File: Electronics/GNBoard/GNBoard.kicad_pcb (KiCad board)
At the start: 2 copper layers, 14 parts, among them P1 Battery, SW1 PowerSwitch, U1 LM2576

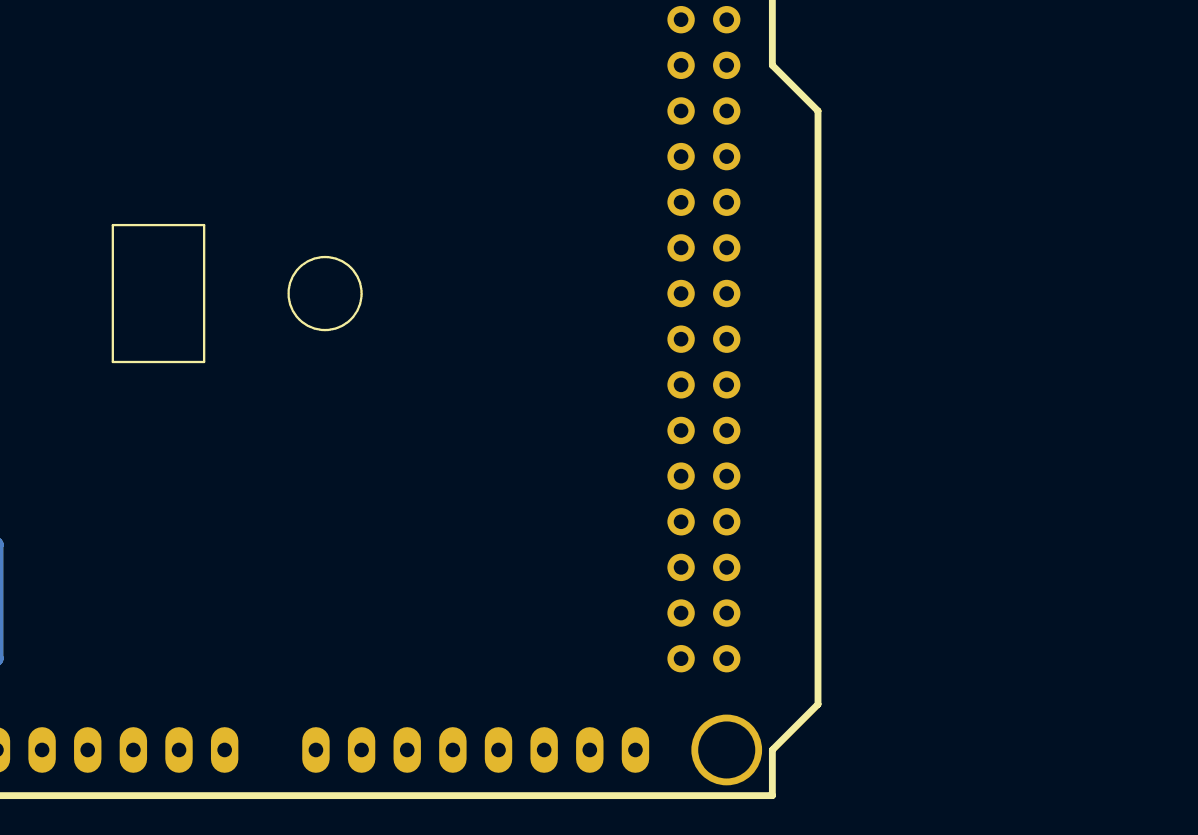
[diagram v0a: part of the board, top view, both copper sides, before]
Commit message: LDR and IR connectors added to schematic
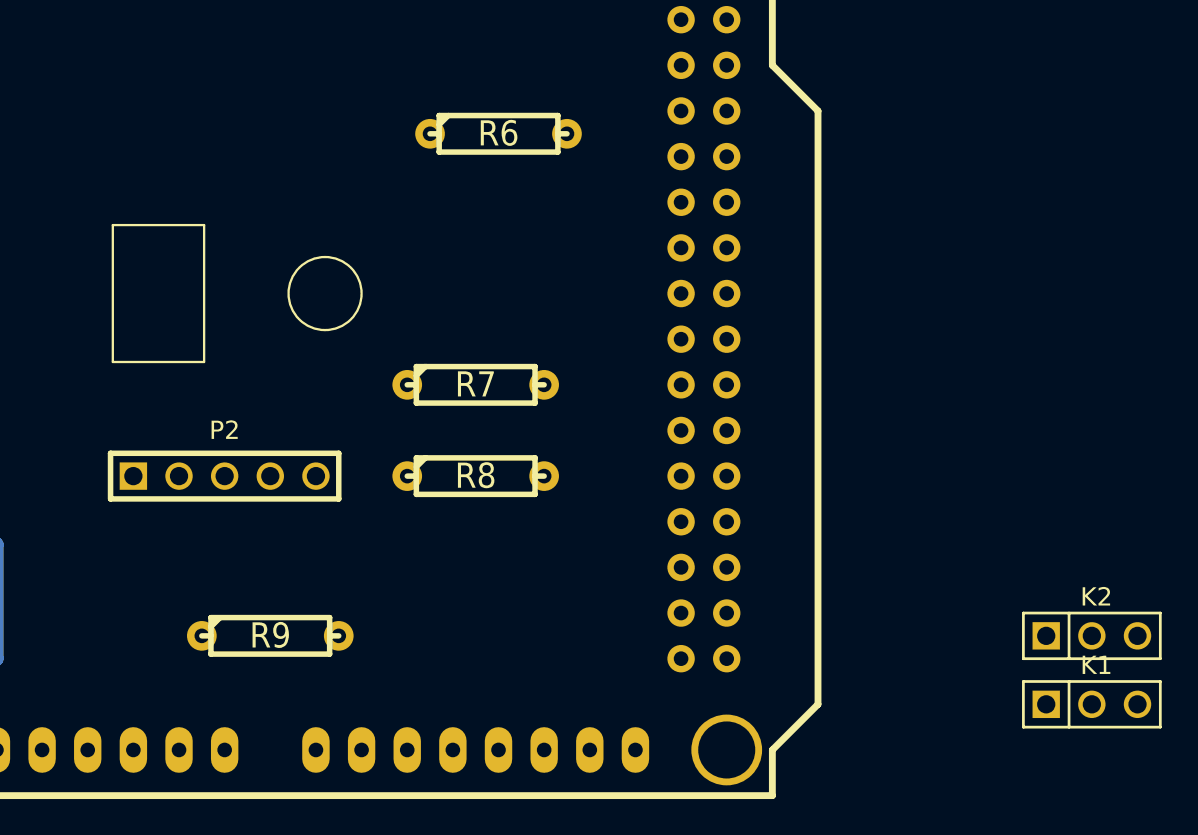
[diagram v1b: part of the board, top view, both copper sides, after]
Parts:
- added K1: IR1, PIN_ARRAY_3X1, F.Cu at (223.5, 118.1)
- added K2: IR2, PIN_ARRAY_3X1, F.Cu at (223.5, 114.3)
- added P2: CONN_5, PIN_ARRAY_5x1, F.Cu at (175.3, 105.4)
- added R6: 33k, R3-LARGE_PADS, F.Cu at (190.5, 86.4)
- added R7: 33k, R3-LARGE_PADS, F.Cu at (189.2, 100.3)
- added R8: 33k, R3-LARGE_PADS, F.Cu at (189.2, 105.4)
- added R9: 33k, R3-LARGE_PADS, F.Cu at (177.8, 114.3)
- R1, R5: value R -> 6k8
- R2, R3, R4: value R -> 330

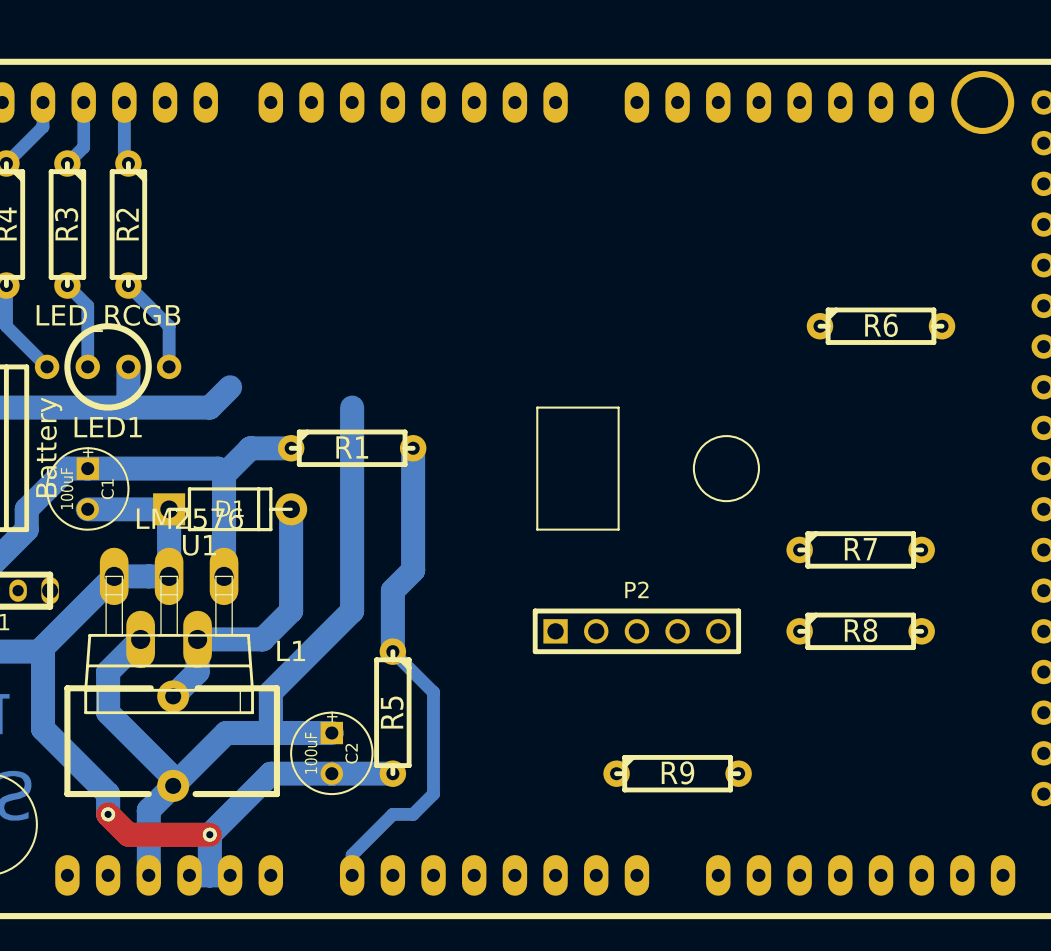
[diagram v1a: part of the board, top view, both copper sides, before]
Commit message: Layout for the LDR
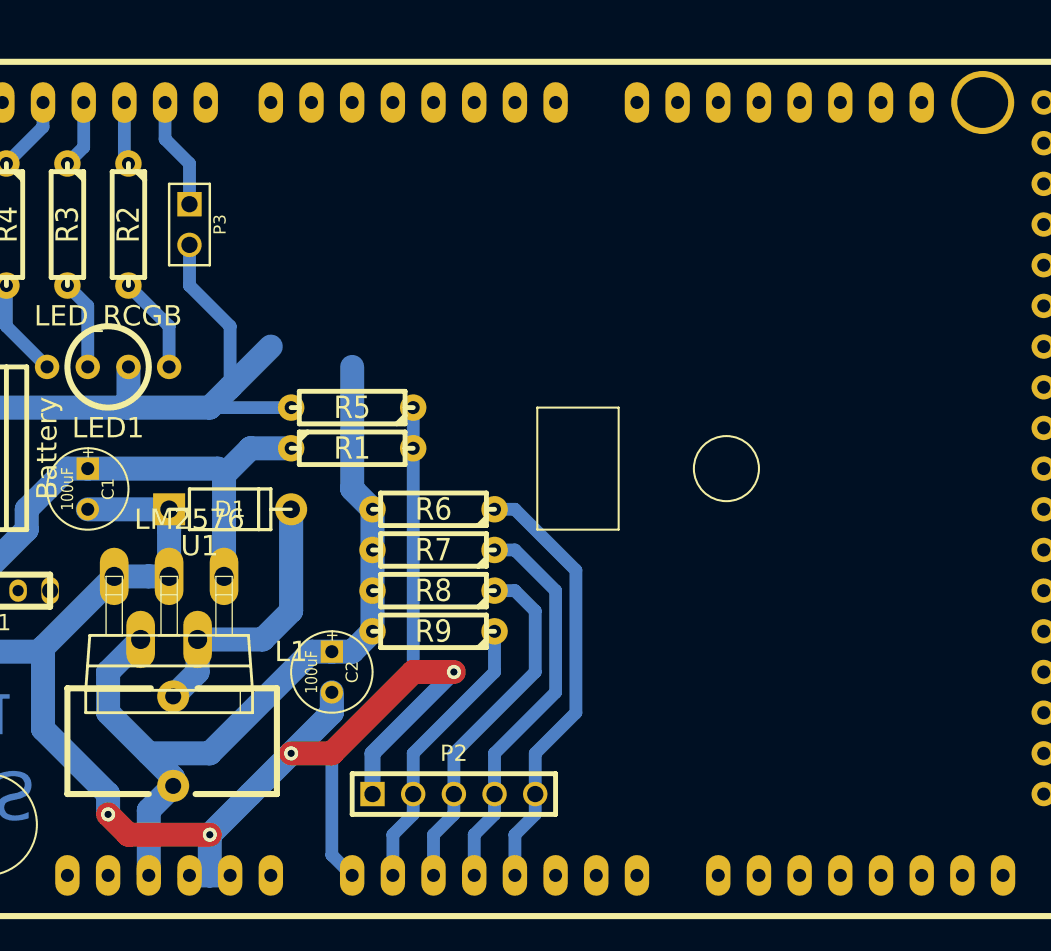
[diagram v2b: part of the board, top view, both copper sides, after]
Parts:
- added P3: Spk, PIN_ARRAY_2X1, F.Cu at (147.3, 80.0)
- moved R6 30.2 mm to (162.6, 97.8), turned to 180 degrees
- moved R8 26.8 mm to (162.6, 102.9), turned to 180 degrees
- moved R7 26.7 mm to (162.6, 100.3), turned to 180 degrees
- moved R5 19.2 mm to (157.5, 91.4), turned to 180 degrees
- moved R9 17.6 mm to (162.6, 105.4), turned to 180 degrees
- moved P2 15.3 mm to (163.8, 115.6)
- moved C2 5.08 mm to (156.2, 108.0)
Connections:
- SHIELD1 pad 9: N-0000046 (its old number) -> Buzzer
- SHIELD1 pad AD1: N-0000065 (its old number) -> LDR1
- SHIELD1 pad AD2: N-0000074 (its old number) -> LDR2
- SHIELD1 pad AD3: N-0000073 (its old number) -> LDR3
- SHIELD1 pad AD4: N-0000071 (its old number) -> LDR4
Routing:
- net GND: track 122.1 -> 161.8 mm, vias 2 -> 4
- net LDR4: track 0.00 -> 27.3 mm
- net LDR3: track 0.00 -> 24.7 mm
- net LDR2: track 0.00 -> 22.2 mm
- net LDR1: track 0.00 -> 17.9 mm
- net Buzzer: track 0.00 -> 6.98 mm
- net BattVolt: track 31.1 -> 31.8 mm
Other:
- net class Default: clearance 0.5 -> 0.4
- rule trace_clearance: 0.5 -> 0.4

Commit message: v0.1 finished
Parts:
- added K10: IR4, PIN_ARRAY_3X1, F.Cu at (179.7, 114.3)
- added K11: CNY_1, PIN_ARRAY_3X1, F.Cu at (173.4, 78.7)
- added K12: CNY_2, PIN_ARRAY_3X1, F.Cu at (175.9, 78.7)
- added K13: CNY_3, PIN_ARRAY_3X1, F.Cu at (178.4, 78.7)
- added K14: CNY_4, PIN_ARRAY_3X1, F.Cu at (181.0, 78.7)
- added K15: CNY_5, PIN_ARRAY_3X1, F.Cu at (183.5, 78.7)
- added K16: CNY_6, PIN_ARRAY_3X1, F.Cu at (186.1, 78.7)
- added K3: SERVO_1, PIN_ARRAY_3X1, F.Cu at (153.7, 78.7)
- added K4: SERVO_2, PIN_ARRAY_3X1, F.Cu at (156.2, 78.7)
- added K5: SERVO_3, PIN_ARRAY_3X1, F.Cu at (158.8, 78.7)
- added K6: SERVO_4, PIN_ARRAY_3X1, F.Cu at (161.3, 78.7)
- added K7: SERVO_5, PIN_ARRAY_3X1, F.Cu at (163.8, 78.7)
- added K8: SERVO_6, PIN_ARRAY_3X1, F.Cu at (166.4, 78.7)
- added K9: IR3, PIN_ARRAY_3X1, F.Cu at (177.2, 114.3)
- added P4: I2C_1, PIN_ARRAY_4x1, F.Cu at (193.7, 76.8)
- added P5: I2C_2, PIN_ARRAY_4x1, F.Cu at (193.7, 85.7)
- added P6: DHT_Conn, PIN_ARRAY_4x1, F.Cu at (191.1, 114.9)
- added R10: R, R3-LARGE_PADS, F.Cu at (193.7, 82.5)
- added R11: R, R3-LARGE_PADS, F.Cu at (193.7, 80.0)
- added R12: 10k, R3-LARGE_PADS, F.Cu at (184.2, 113.7)
- added SW2: SW_PUSH, SW_PUSH_SMALL, F.Cu at (134.6, 81.3)
- added SW3: SW_PUSH, SW_PUSH_SMALL, F.Cu at (133.3, 113.7)
- moved K1 51.6 mm to (172.1, 114.3), turned to 90 degrees
- moved K2 48.9 mm to (174.6, 114.3), turned to 90 degrees
- moved P2 20.7 mm to (167.6, 95.2), turned to 90 degrees
- moved R5 8.03 mm to (149.9, 88.9), turned to 225 degrees
- moved R6 7.73 mm to (161.3, 90.2)
- moved R7 7.73 mm to (161.3, 92.7)
- moved R8 7.73 mm to (161.3, 95.2)
- moved R9 7.73 mm to (161.3, 97.8)
- moved R1 6.35 mm to (152.4, 90.2), turned to 45 degrees
- moved R4 5.08 mm to (141.0, 80.0)
- moved R3 3.81 mm to (143.5, 80.0)
- moved P3 3.59 mm to (149.9, 77.5)
- moved R2 2.54 mm to (146.1, 80.0)
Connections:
- SHIELD1 pad 10: LedR -> LedG
- SHIELD1 pad 11: LedG -> LedB
- SHIELD1 pad 12: LedB -> Button1
- SHIELD1 pad 14: N-0000023 -> CNY1
- SHIELD1 pad 15: N-0000059 -> CNY2
- SHIELD1 pad 16: N-0000055 -> CNY3
- SHIELD1 pad 17: N-0000051 (its old number) -> CNY4
- SHIELD1 pad 18: N-0000047 (its old number) -> CNY5
- SHIELD1 pad 19: N-0000043 -> CNY6
- SHIELD1 pad 2: N-0000060 (its old number) -> Servo6
- SHIELD1 pad 20: N-0000061 -> I2C_SDA
- SHIELD1 pad 21: N-0000036 (its old number) -> I2C_SCL
- SHIELD1 pad 3: N-0000067 -> Servo5
- SHIELD1 pad 4: N-0000066 (its old number) -> Servo4
- SHIELD1 pad 5: N-0000065 -> Servo3
- SHIELD1 pad 6: N-0000064 (its old number) -> Servo2
- SHIELD1 pad 7: N-0000063 -> Servo1
- SHIELD1 pad 8: N-0000062 -> Buzzer
- SHIELD1 pad 9: Buzzer -> LedR
- SHIELD1 pad AD5: N-0000081 -> V_IR1
- SHIELD1 pad AD6: N-0000080 -> V_IR2
- SHIELD1 pad AD7: N-0000079 -> V_IR3
- SHIELD1 pad AD8: N-0000071 (its old number) -> V_IR4
- SHIELD1 pad AD9: N-0000078 (its old number) -> DHTpin
- SHIELD1 pad RST: N-0000077 (its old number) -> ResetB
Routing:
- net GND: track 161.8 -> 345.6 mm
- net +5V: track 52.1 -> 196.1 mm
- net I2C_SCL: track 0.00 -> 16.1 mm
- net I2C_SDA: track 0.00 -> 15.2 mm
- net DHTpin: track 0.00 -> 14.1 mm
- net LDR1: track 17.9 -> 31.4 mm
- net BattVolt: track 31.8 -> 44.8 mm
- net LDR4: track 27.3 -> 39.0 mm
- net LDR3: track 24.7 -> 36.5 mm
- net LDR2: track 22.2 -> 33.9 mm
- net Button1: track 0.00 -> 5.50 mm
- net V_IR1: track 0.00 -> 5.34 mm
- net ResetB: track 0.00 -> 5.13 mm
- net V_IR3: track 0.00 -> 4.60 mm
- net V_IR2: track 0.00 -> 4.60 mm
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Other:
- board outline added: 78.1 x 54.6 mm
- net class Default: via_dia 0.889 -> 1.5; via_drill 0.635 -> 0.6
- board text added: "CGS 2013"
- board text removed: "CGS"

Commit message: Added decoupling caps
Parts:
- added C3: 100uF, C1V7, F.Cu at (196.2, 91.4)
- added C4: 100uF, C1V7, F.Cu at (178.4, 87.0)
- added C5: 100uF, C1V7, F.Cu at (176.5, 106.7)
- added C6: 100uF, C1V7, F.Cu at (181.0, 137.2)
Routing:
- net +5V: track 196.1 -> 207.5 mm
- net GND: track 345.6 -> 351.6 mm

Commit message: Finished first version, added schematics
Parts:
- removed C6: 100uF, C1V7
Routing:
- net +5V: track 207.5 -> 208.1 mm
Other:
- outline, holes or cut-outs redrawn

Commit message: First tests, added source code
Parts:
- C2: value 100uF -> 1000uF; footprint C1V5 -> C1V8
- moved C2 1.27 mm to (157.5, 108.0)
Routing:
- net +5V: track 208.1 -> 208.7 mm
- net GND: track 351.6 -> 352.1 mm
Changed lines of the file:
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@@
     (links 123)
     (no_connects 5)
-    (area 104.010934 64.7256 208.870501 124.015501)
+    (area 125.539499 69.024499 204.025501 124.015501)
     (thickness 1.6)
     (drawings 10)
@@
   )
   (setup
-    (last_trace_width 0.8)
+    (last_trace_width 1.5)
     (user_trace_width 1)
     (user_trace_width 1.5)
@@
   )
   (module C1V5 (layer Comp.)
-    (at 156.21 107.95 270)
-    (descr "Condensateur e = 1 pas")
-    (tags C)
-    (fp_text reference C2 (at 0 -1.26746 270) (layer F.SilkS)
-      (effects (font (size 0.762 0.762) (thickness 0.127)))
-    )
-    (fp_text value 100uF (at 0 1.27 270) (layer F.SilkS)
-      (effects (font (size 0.762 0.635) (thickness 0.127)))
-    )
-    (fp_text user + (at -2.286 0 270) (layer F.SilkS)
-      (effects (font (size 0.762 0.762) (thickness 0.2032)))
-    )
-    (fp_circle (center 0 0) (end 0.127 -2.54) (layer F.SilkS) (width 0.127))
-    (pad 1 thru_hole rect (at -1.27 0 270) (size 1.397 1.397) (drill 0.8128)
-      (layers *.Cu *.Mask F.SilkS)
-      (net 1 +5V)
-    )
-    (pad 2 thru_hole circle (at 1.27 0 270) (size 1.397 1.397) (drill 0.8128)
-      (layers *.Cu *.Mask F.SilkS)
-      (net 13 GND)
-    )
-    (model discret/c_vert_c1v5.wrl
-      (at (xyz 0 0 0))
-      (scale (xyz 1 1 1))
-      (rotate (xyz 0 0 0))
-    )
-  )
-  (module C1V5 (layer Comp.)
     (at 140.97 96.52 270)
     (descr "Condensateur e = 1 pas")
@@
     )
   )
+  (module C1V8 (layer Comp.)
+    (at 157.48 107.95 270)
+    (fp_text reference C2 (at 0 2.032 270) (layer F.SilkS)
+      (effects (font (size 1.016 0.889) (thickness 0.2032)))
+    )
+    (fp_text value 1000uF (at 0 -1.77546 270) (layer F.SilkS)
+      (effects (font (size 1.016 0.889) (thickness 0.2032)))
+    )
+    (fp_text user + (at -3.04546 0 270) (layer F.SilkS)
+      (effects (font (thickness 0.2032)))
+    )
+    (fp_circle (center 0 0) (end 4.064 0) (layer F.SilkS) (width 0.2032))
+    (pad 1 thru_hole rect (at -1.27 0 270) (size 1.651 1.651) (drill 0.8128)
+      (layers *.Cu *.Mask F.SilkS)
+      (net 1 +5V)
+    )
+    (pad 2 thru_hole circle (at 1.27 0 270) (size 1.651 1.651) (drill 0.8128)
+      (layers *.Cu *.Mask F.SilkS)
+      (net 13 GND)
+    )
+    (model discret/c_vert_c1v8.wrl
+      (at (xyz 0 0 0))
+      (scale (xyz 1 1 1))
+      (rotate (xyz 0 0 0))
+    )
+  )
   (gr_line (start 125.73 123.825) (end 125.73 98.425) (angle 90) (layer Edge.Cuts) (width 0.381))
   (gr_line (start 203.835 123.825) (end 203.835 97.155) (angle 90) (layer Edge.Cuts) (width 0.381))
@@
     (effects (font (size 2.5 2) (thickness 0.4)) (justify mirror))
   )
+  (segment (start 157.48 106.68) (end 156.21 105.41) (width 1.5) (layer Cobre) (net 1) (status 400000))
   (segment (start 177.8 106.68) (end 179.705 106.68) (width 1.5) (layer Cobre) (net 1))
   (segment (start 177.165 111.76) (end 177.165 111.125) (width 1.5) (layer Cobre) (net 1))
@@
   (segment (start 157.48 97.79) (end 157.48 99.06) (width 1.5) (layer Cobre) (net 1))
   (segment (start 157.48 99.06) (end 157.48 104.14) (width 1.5) (layer Cobre) (net 1))
-  (segment (start 157.48 104.14) (end 154.94 106.68) (width 1.5) (layer Cobre) (net 1))
-  (segment (start 156.21 106.68) (end 154.94 106.68) (width 1.5) (layer Cobre) (net 1))
+  (segment (start 157.48 104.14) (end 156.21 105.41) (width 1.5) (layer Cobre) (net 1))
+  (segment (start 156.21 105.41) (end 154.94 106.68) (width 1.5) (layer Cobre) (net 1))
   (segment (start 148.59 113.03) (end 144.78 113.03) (width 1.5) (layer Cobre) (net 1))
   (segment (start 154.94 106.68) (end 148.59 113.03) (width 1.5) (layer Cobre) (net 1))
@@
   (segment (start 191.77 117.475) (end 184.15 117.475) (width 0.8) (layer Cobre) (net 12))
   (segment (start 192.405 116.84) (end 191.77 117.475) (width 0.8) (layer Cobre) (net 12))
+  (segment (start 157.48 109.22) (end 154.94 111.76) (width 1.5) (layer Cobre) (net 13) (status 400000))
   (segment (start 179.705 86.995) (end 184.15 86.995) (width 1.5) (layer Cobre) (net 13))
   (segment (start 175.26 106.68) (end 174.625 106.045) (width 1.5) (layer Cobre) (net 13))
@@
   (segment (start 165.1 101.6) (end 166.37 101.6) (width 1.5) (layer Cobre) (net 13))
   (segment (start 166.37 101.6) (end 167.64 100.33) (width 1.5) (layer Cobre) (net 13))
-  (segment (start 156.21 109.22) (end 156.21 110.49) (width 1.5) (layer Cobre) (net 13))
-  (segment (start 156.21 110.49) (end 154.94 111.76) (width 1.5) (layer Cobre) (net 13))
   (segment (start 154.94 111.76) (end 153.67 113.03) (width 1.5) (layer Cobre) (net 13))
   (segment (start 153.67 113.03) (end 151.765 114.935) (width 1.5) (layer Cobre) (net 13))

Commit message: Improvements for the GNBoard
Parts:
- SW1: footprint MICROSWITCH_SPST -> SWITCH_3Pin
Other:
- board size 78.1 x 54.6 mm -> 77.9 x 54.5 mm
